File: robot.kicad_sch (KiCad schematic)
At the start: 21 parts, among them J3 Programming, J5 Switches, SW1 Reset, SW2 Action, SW3 KILL, SW4 Flash, SW6 OPTION, U1 ESP32-WROOM-32D

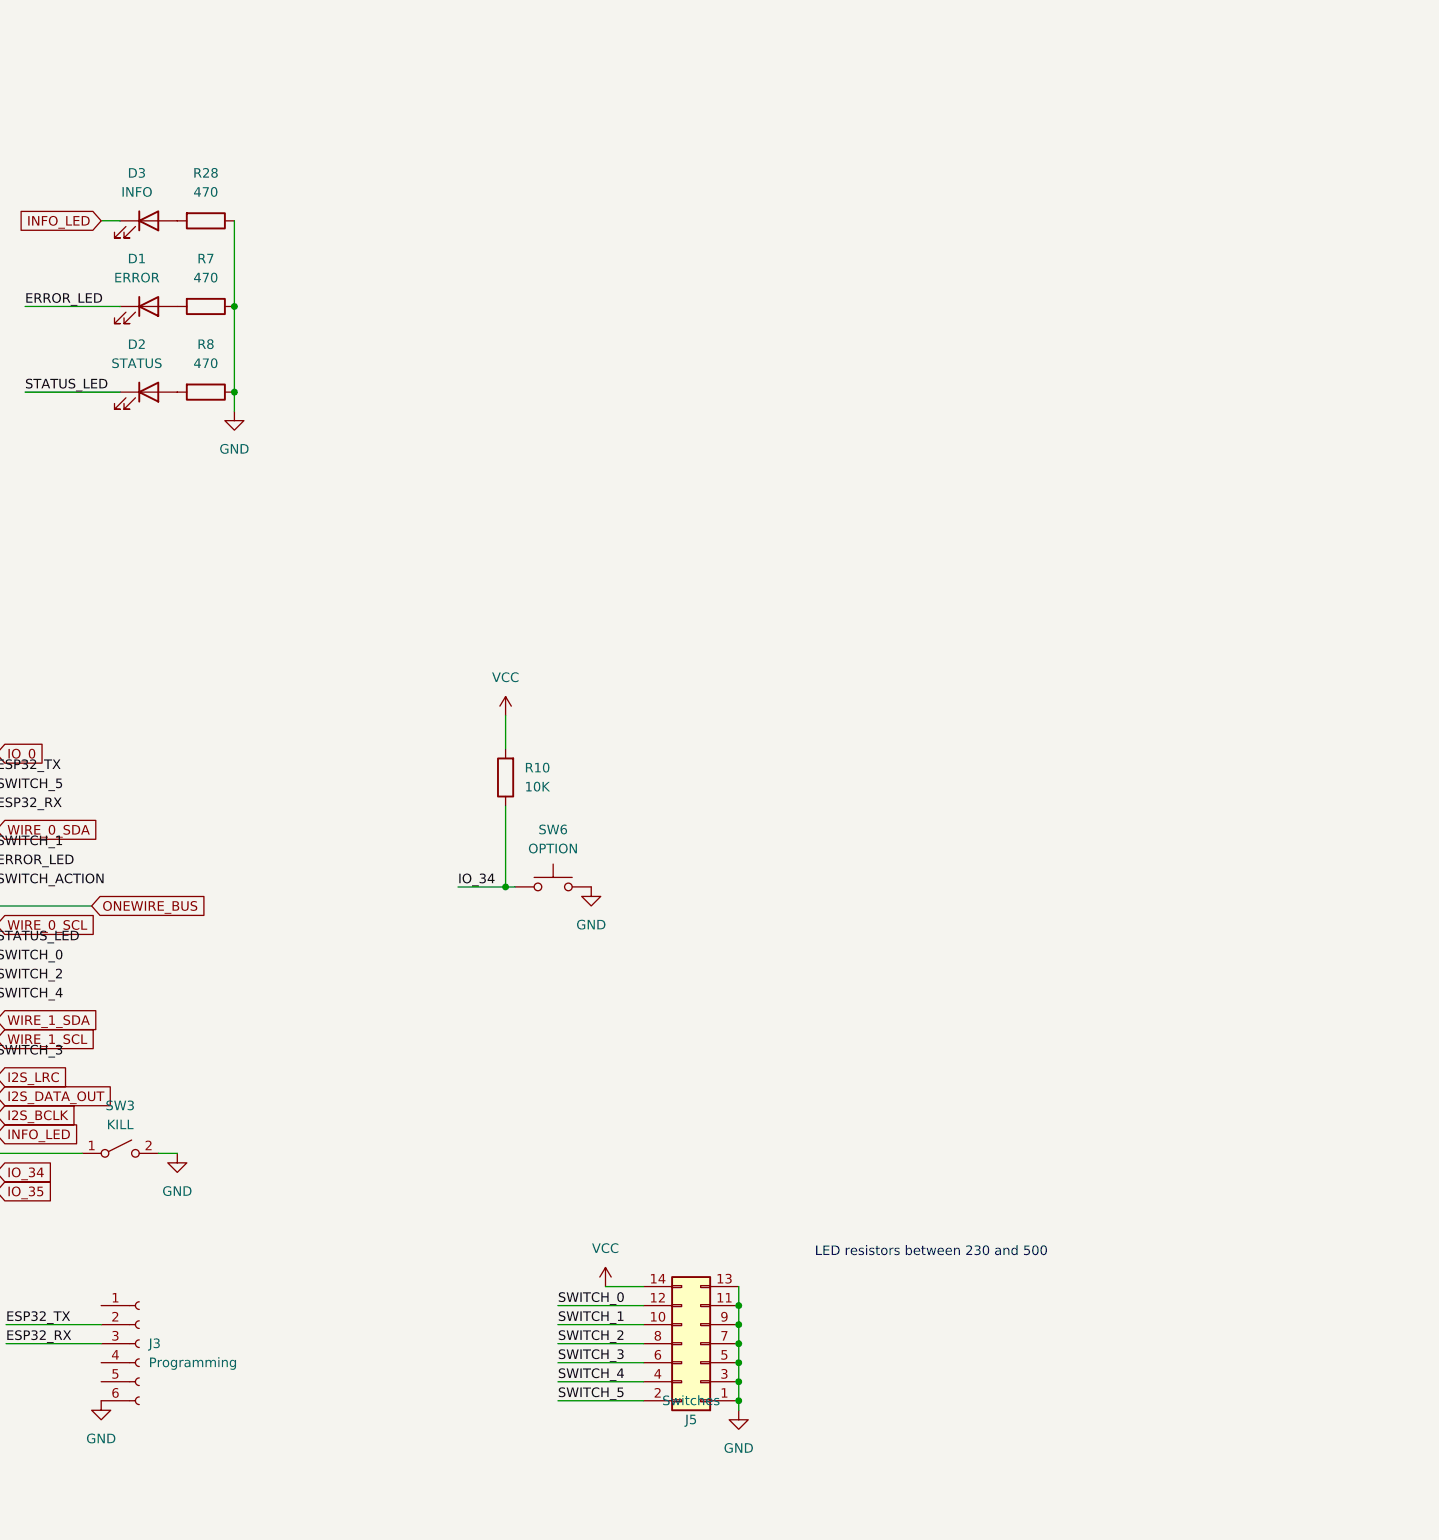
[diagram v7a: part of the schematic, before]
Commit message: Upgrade to version 7, started adding new WROOM-S3
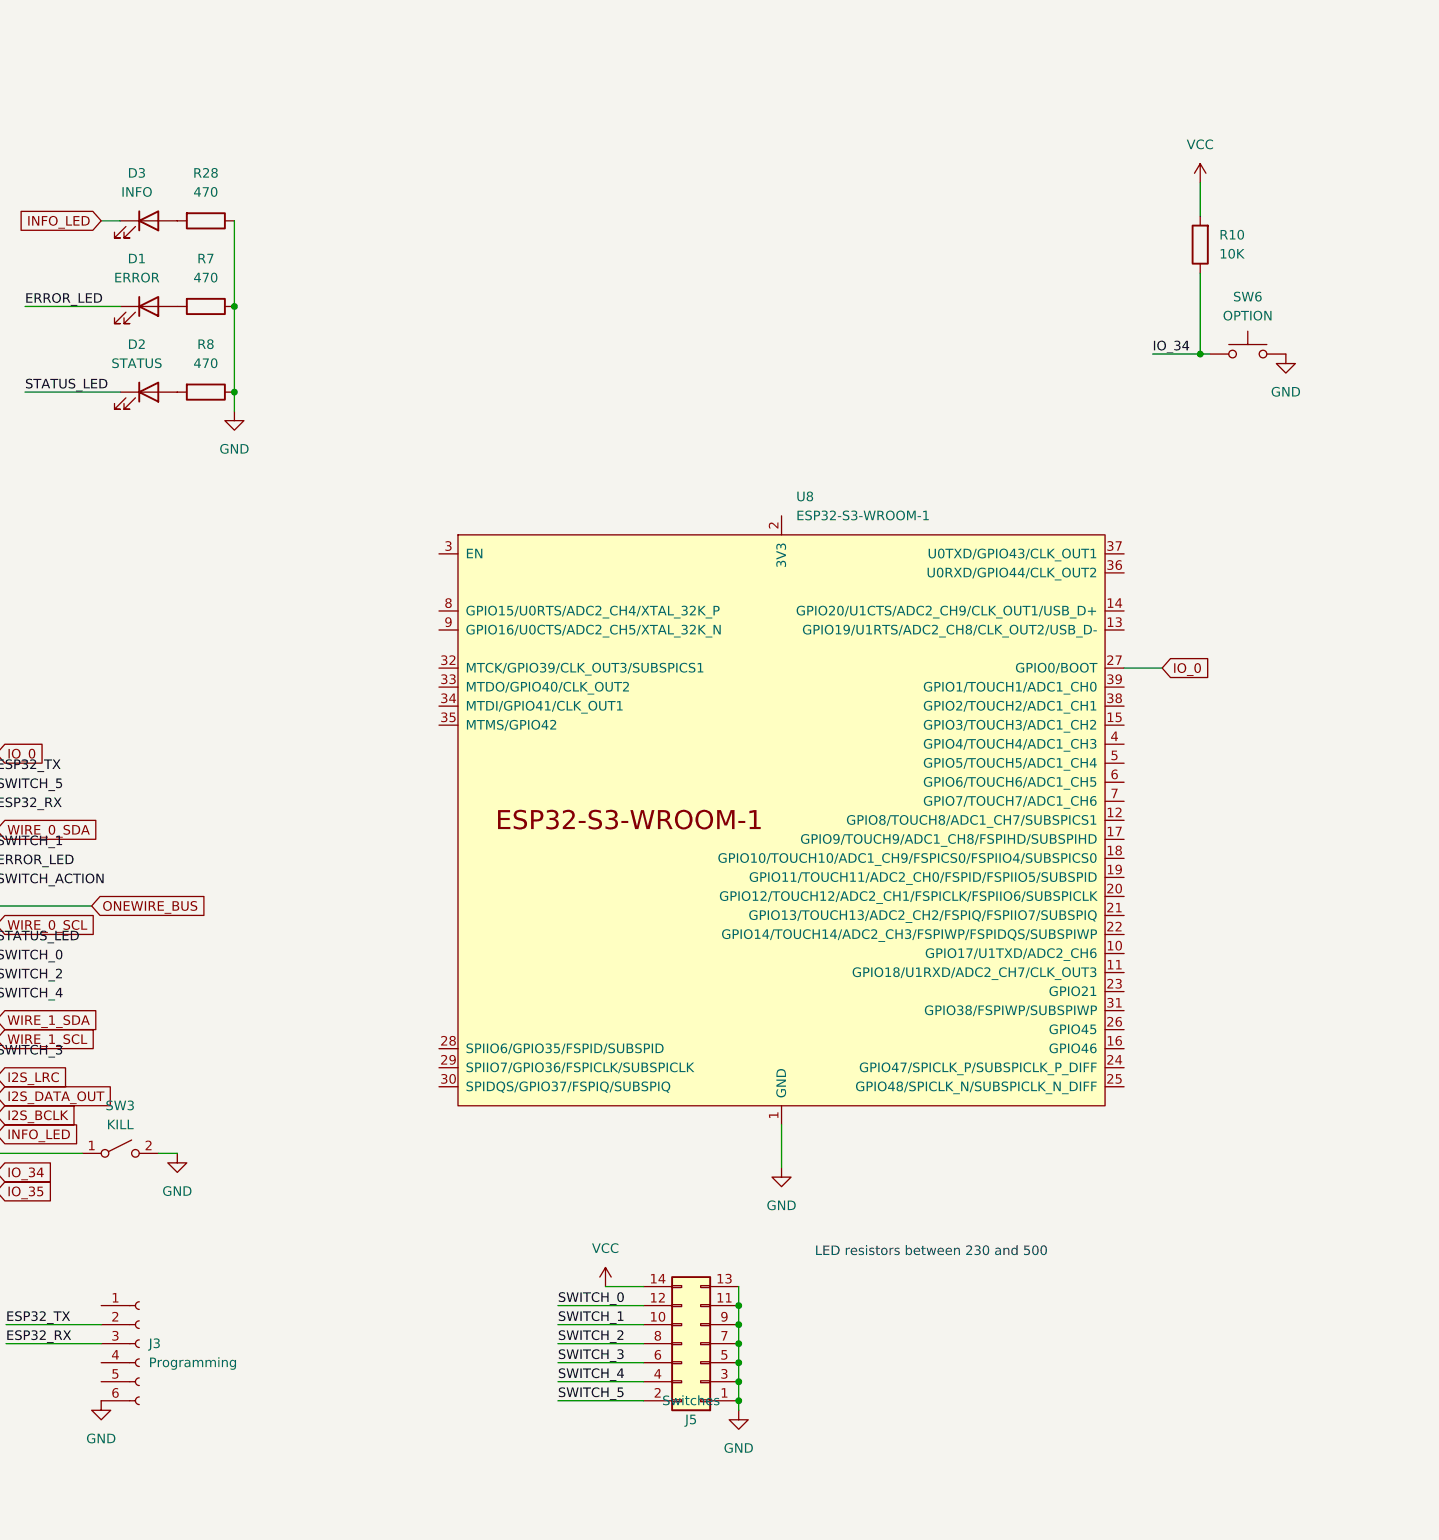
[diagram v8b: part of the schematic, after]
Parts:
- added U8: ESP32-S3-WROOM-1, PCM_Espressif:ESP32-S3-WROOM-1U, symbol PCM_Espressif:ESP32-S3-WROOM-1
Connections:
- net GND: now also U8.1 (GND), U8.40 (GND), U8.41 (GND)
- net IO_0: now also U8.27 (GPIO0/BOOT)
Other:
- moved on the sheet: R10, SW6
